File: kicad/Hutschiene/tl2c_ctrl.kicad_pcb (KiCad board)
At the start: 4 copper layers, 67 x 57 mm, 57 parts, among them IC101 ATTINY20-X, P102 RJ45, P103 CTL CONN, P104 TPI Header, P107 CTL PWR, P109 5VDC, P201 Mode_Bridge, Q301 IRLML2502, Q302 IRLML2502, Q303 IRLML2502, SW101 TL3315NF160Q, U201 LF120ABDT-TR, U202 TPS70933

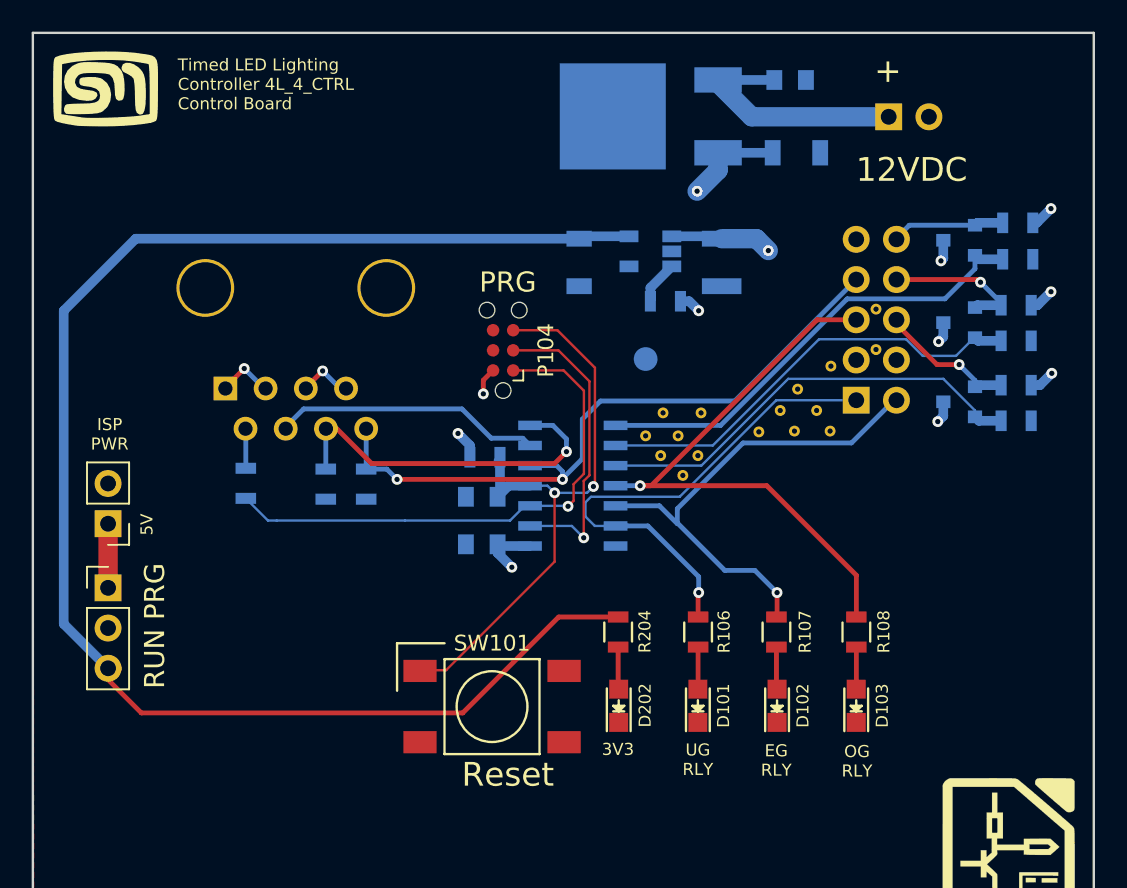
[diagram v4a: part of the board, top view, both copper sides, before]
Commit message: Corrected issues with the connectors - Pushing to OSH Park
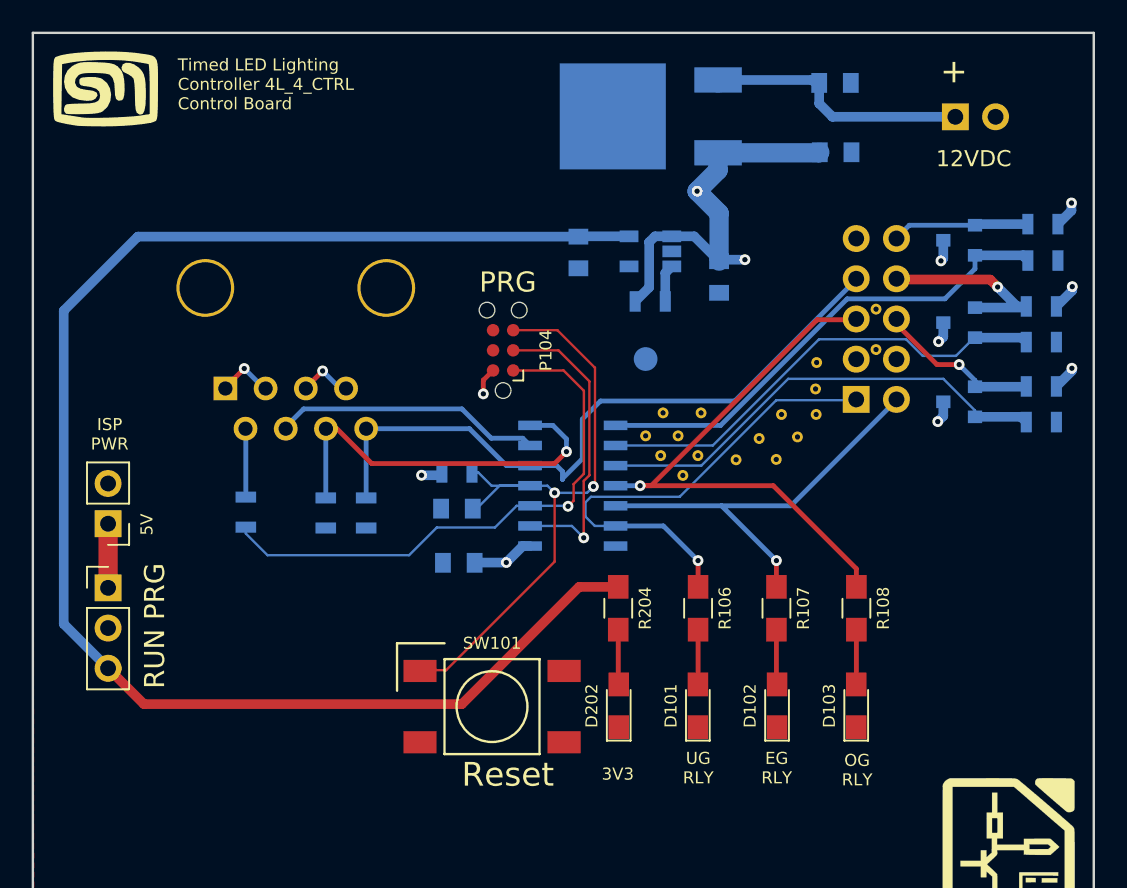
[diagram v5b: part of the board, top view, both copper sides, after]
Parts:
- removed the REF**31 at (204.2, 98.5)
- removed the REF**31 at (201.9, 98.5)
- removed the REF**31 at (200.6, 99.8)
- removed the REF**31 at (205.1, 95.7)
- removed the REF**31 at (203.0, 97.1)
- removed the REF**31 at (205.1, 99.8)
- removed the REF**31 at (202.8, 99.8)
- added REF**31: Stitch_VIA, tl2c-footprint:Stitch_VIA, F.Cu at (199.1, 101.6)
- added REF**31: Stitch_VIA, tl2c-footprint:Stitch_VIA, F.Cu at (201.7, 101.5)
- added REF**31: Stitch_VIA, tl2c-footprint:Stitch_VIA, F.Cu at (200.6, 100.2)
- added REF**31: Stitch_VIA, tl2c-footprint:Stitch_VIA, F.Cu at (203.0, 100.1)
- added REF**31: Stitch_VIA, tl2c-footprint:Stitch_VIA, F.Cu at (204.2, 98.7)
- added REF**31: Stitch_VIA, tl2c-footprint:Stitch_VIA, F.Cu at (202.0, 98.7)
- added REF**31: Stitch_VIA, tl2c-footprint:Stitch_VIA, F.Cu at (204.1, 97.1)
- added REF**31: Stitch_VIA, tl2c-footprint:Stitch_VIA, F.Cu at (204.2, 95.4)
- C202: footprint Capacitors_SMD:C_1210 -> Capacitors_SMD:C_0805
- C203, C204: footprint Capacitors_SMD:C_1206 -> Capacitors_SMD:C_0805
- D101, D102, D103, D202: footprint LEDs:LED_0805 -> LEDs:LED_0805_HandSoldering
- R106, R107, R108, R204: footprint Resistors_SMD:R_0805 -> Resistors_SMD:R_0805_HandSoldering
- moved P107 4.21 mm to (213.0, 79.9)
- moved C201 2.84 mm to (205.4, 77.8)
- moved C203 2.48 mm to (205.4, 82.1)
- moved R101 2.01 mm to (181.5, 102.4)
- moved C101 1.86 mm to (181.6, 108.1)
- moved R103 1.82 mm to (168.2, 104.9)
- moved R104 1.82 mm to (173.2, 104.9)
- moved R105 1.82 mm to (175.8, 104.9)
- moved C102 1.74 mm to (181.5, 104.6)
- moved R309 1.59 mm to (218.5, 86.7)
- moved R303 1.59 mm to (218.5, 89.0)
- moved R301 1.59 mm to (218.4, 99.2)
- moved R307 1.59 mm to (218.4, 96.9)
- moved R302 1.59 mm to (218.4, 94.1)
- moved R308 1.59 mm to (218.4, 91.9)
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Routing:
- net /PIR13/U+: track 19.2 -> 30.4 mm, vias 6 -> 5
- net /RelayEG: track 32.1 -> 27.5 mm
- net /~Reset: track 40.1 -> 43.3 mm
- net /PIR13/PIR_EG: track 9.08 -> 12.2 mm
- net /RelayUG: track 32.7 -> 30.6 mm
- net /SDA: track 2.51 -> 4.33 mm
- net /RLY_INT: track 22.4 -> 24.2 mm
- net /PIR13/PIR_UG: track 8.53 -> 10.2 mm
- net /RelayOG: track 39.0 -> 37.3 mm
- net /TPIDATA: track 34.0 -> 35.7 mm
- net /PIR13/SIG_UG: track 28.0 -> 29.6 mm
- net /PIR13/SIG_OG: track 29.5 -> 31.1 mm
- net /PIR13/SIG_EG: track 28.1 -> 29.7 mm
- net /PIR13/PIR_OG: track 7.19 -> 8.74 mm
- net /Power System/U+In: track 15.7 -> 17.0 mm
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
